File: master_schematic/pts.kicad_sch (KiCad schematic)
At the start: 27 parts, among them J10 0430450400, J2 0430450400, J3 0430450400, J4 0430450400, J5 0430450400, J6 0430450400, J7 0430450400, J8 0430450400, J9 0430450400

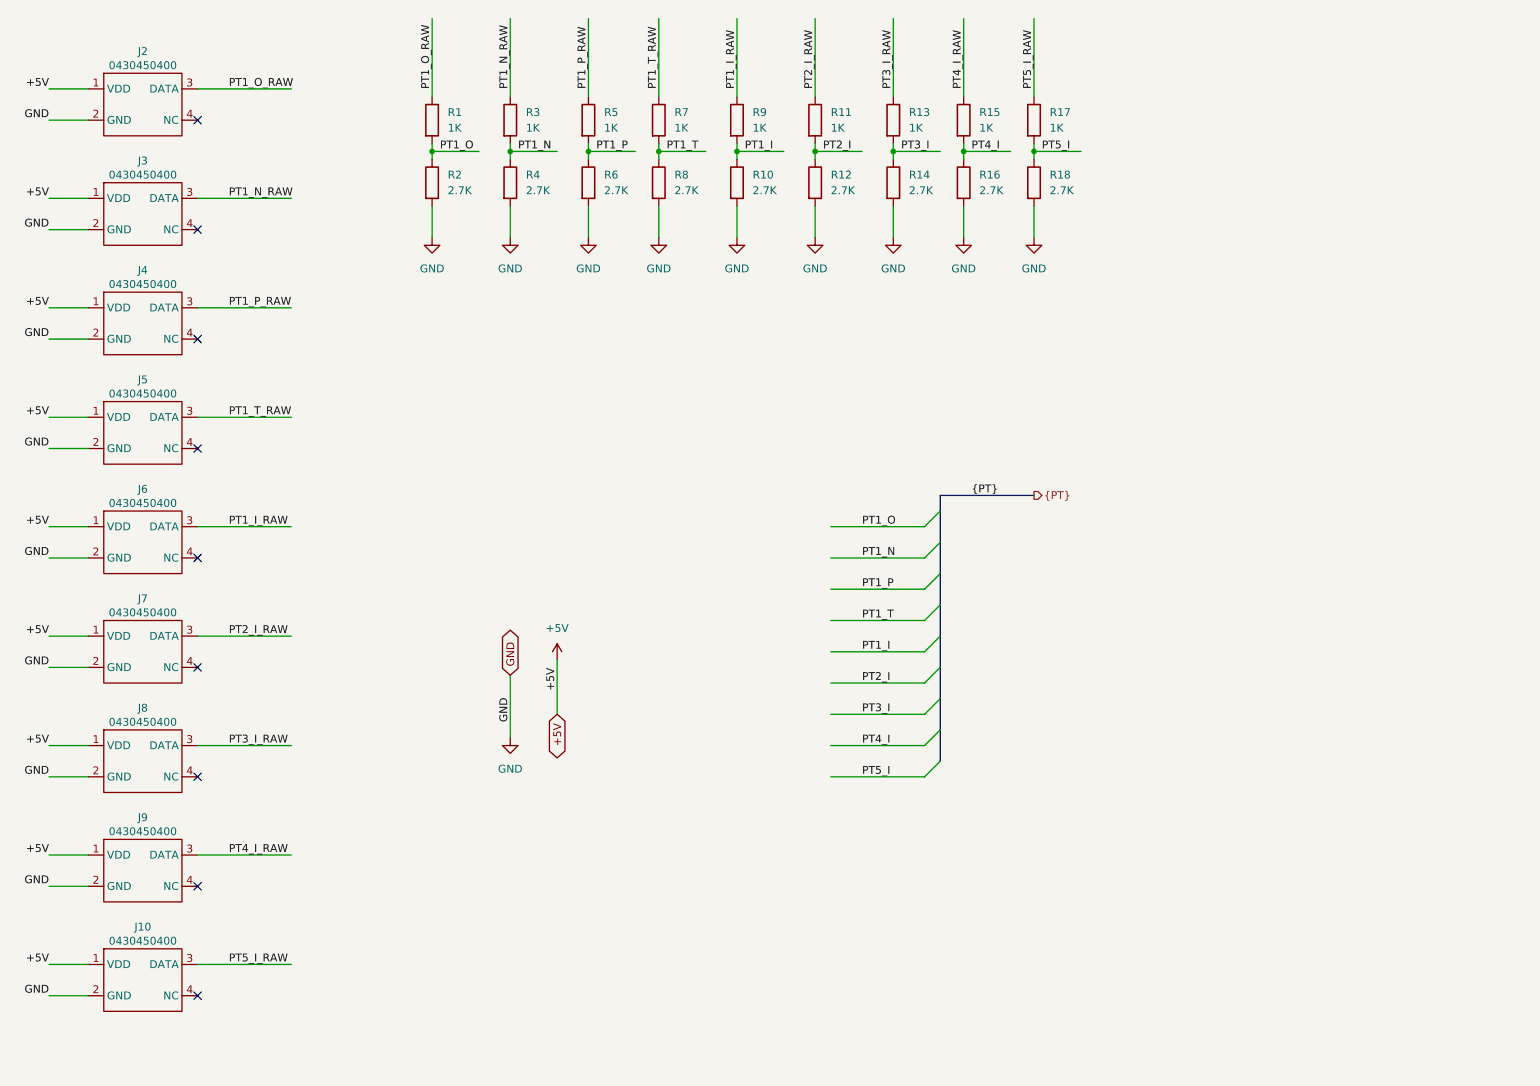
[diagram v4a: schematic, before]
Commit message: added decoupling capacitors, fixed voltage values for TTs and load cells to +3V3
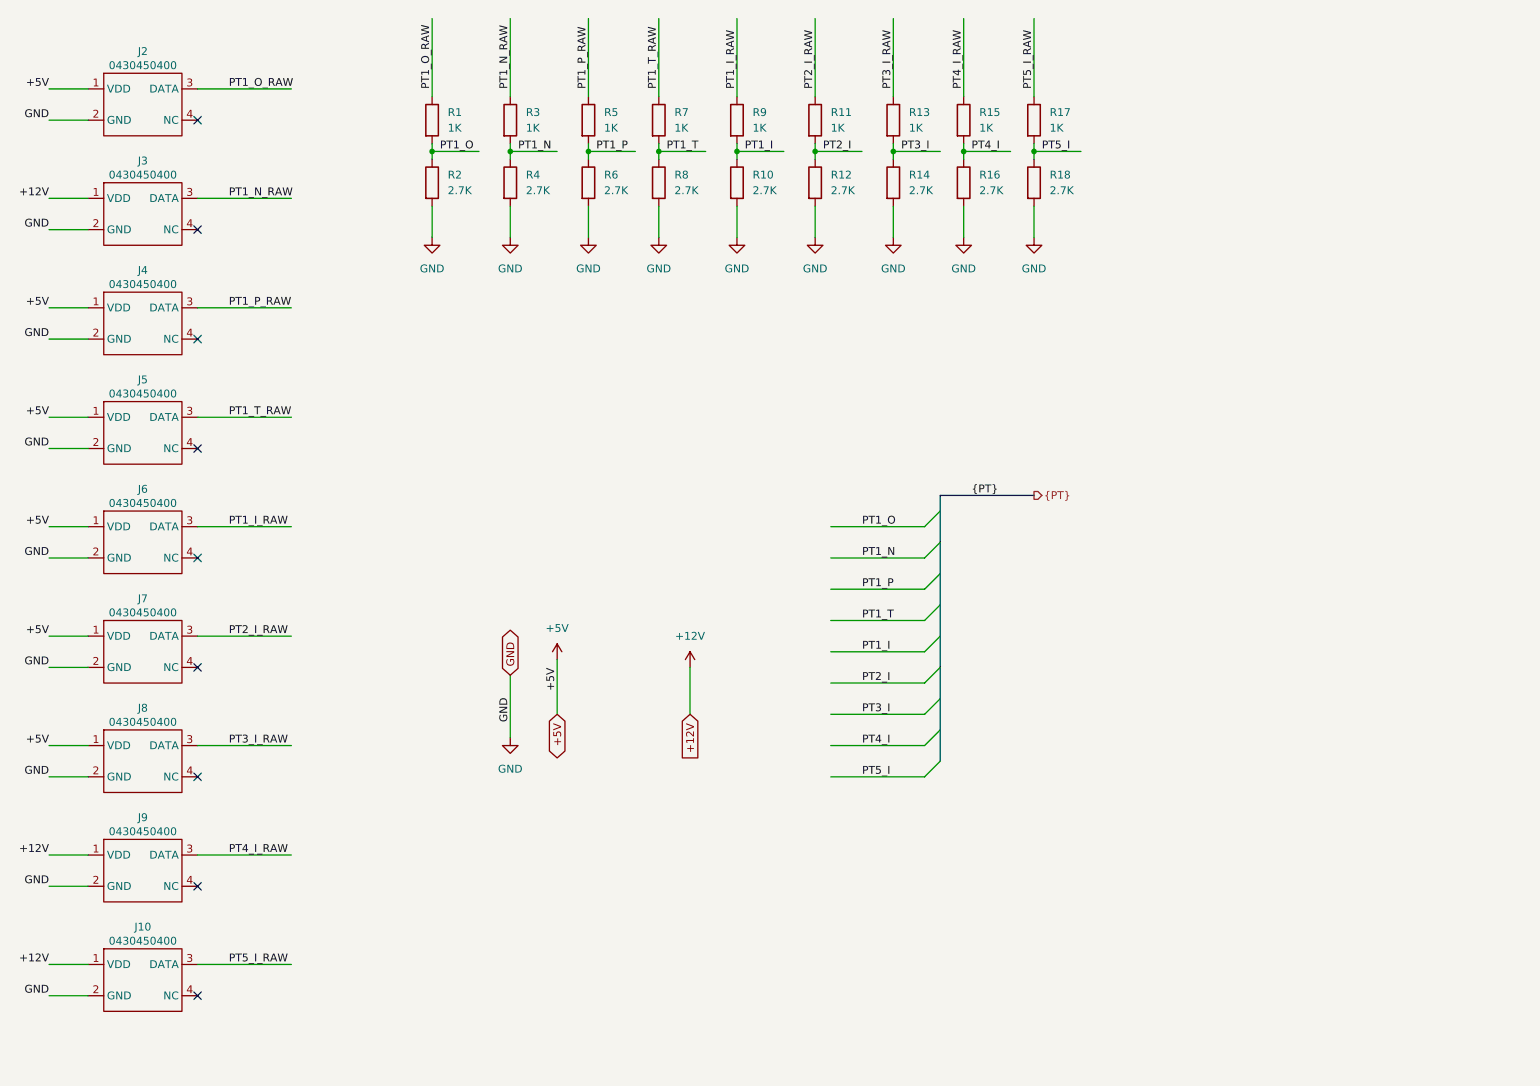
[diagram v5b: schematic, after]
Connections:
- net +5V: no longer J10.1 (VDD), J3.1 (VDD), J9.1 (VDD)
- new net +12V: J10.1 (VDD), J3.1 (VDD), J9.1 (VDD)
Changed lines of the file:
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@@
 	(wire
 		(pts
+			(xy 144.78 125.73) (xy 144.78 133.35)
+		)
+		(stroke
+			(width 0)
+			(type default)
+		)
+	)
+	(wire
+		(pts
 			(xy 177.8 20.32) (xy 177.8 33.02)
 		)
@@
 		)
 	)
-	(label "+5V"
+	(label "+12V"
 		(at 40.64 49.53 180)
 		(fields_autoplaced yes)
@@
 		)
 	)
-	(label "+5V"
+	(label "+12V"
 		(at 40.64 156.21 180)
 		(fields_autoplaced yes)
@@
 		)
 	)
-	(label "+5V"
+	(label "+12V"
 		(at 40.64 173.99 180)
 		(fields_autoplaced yes)
@@
 		)
 	)
+	(global_label "+12V"
+		(shape input)
+		(at 144.78 133.35 270)
+		(fields_autoplaced yes)
+		(effects
+			(font
+				(size 1.27 1.27)
+			)
+			(justify right)
+		)
+		(property "Intersheetrefs" "${INTERSHEET_REFS}"
+			(at 144.78 141.4152 90)
+			(effects
+				(font
+					(size 1.27 1.27)
+				)
+				(justify right)
+				(hide yes)
+			)
+		)
+	)
 	(global_label "+5V"
 		(shape bidirectional)
@@
 		(dnp no)
 		(fields_autoplaced yes)
-		(property "Reference" "#PWR024"
+		(property "Reference" "#PWR027"
 			(at 189.23 62.23 0)
 			(effects
@@
 			(project "master_schematic"
 				(path "/c4f7e98c-e88d-49cc-9841-b70710a90a72/666fb9f9-c631-4136-ad00-30a1b375897d"
-					(reference "#PWR024")
+					(reference "#PWR027")
 					(unit 1)
 				)
@@
 		(dnp no)
 		(fields_autoplaced yes)
-		(property "Reference" "#PWR022"
+		(property "Reference" "#PWR025"
 			(at 165.1 62.23 0)
 			(effects
@@
 			(project "master_schematic"
 				(path "/c4f7e98c-e88d-49cc-9841-b70710a90a72/666fb9f9-c631-4136-ad00-30a1b375897d"
-					(reference "#PWR022")
+					(reference "#PWR025")
 					(unit 1)
 				)
@@
 		(dnp no)
 		(fields_autoplaced yes)
-		(property "Reference" "#PWR021"
+		(property "Reference" "#PWR024"
 			(at 152.4 62.23 0)
 			(effects
@@
 			(project "master_schematic"
 				(path "/c4f7e98c-e88d-49cc-9841-b70710a90a72/666fb9f9-c631-4136-ad00-30a1b375897d"
-					(reference "#PWR021")
+					(reference "#PWR024")
 					(unit 1)
 				)
@@
 		(dnp no)
 		(fields_autoplaced yes)
-		(property "Reference" "#PWR020"
+		(property "Reference" "#PWR022"
 			(at 139.7 62.23 0)
 			(effects
@@
 			(project "master_schematic"
 				(path "/c4f7e98c-e88d-49cc-9841-b70710a90a72/666fb9f9-c631-4136-ad00-30a1b375897d"
-					(reference "#PWR020")
+					(reference "#PWR022")
 					(unit 1)
 				)
@@
 		(dnp no)
 		(fields_autoplaced yes)
-		(property "Reference" "#PWR018"
+		(property "Reference" "#PWR020"
 			(at 123.19 128.27 0)
 			(effects
@@
 			(project "master_schematic"
 				(path "/c4f7e98c-e88d-49cc-9841-b70710a90a72/666fb9f9-c631-4136-ad00-30a1b375897d"
-					(reference "#PWR018")
+					(reference "#PWR020")
 					(unit 1)
 				)
@@
 		(dnp no)
 		(fields_autoplaced yes)
-		(property "Reference" "#PWR016"
+		(property "Reference" "#PWR018"
 			(at 115.57 62.23 0)
 			(effects
@@
 			(project "master_schematic"
 				(path "/c4f7e98c-e88d-49cc-9841-b70710a90a72/666fb9f9-c631-4136-ad00-30a1b375897d"
-					(reference "#PWR016")
+					(reference "#PWR018")
 					(unit 1)
 				)
@@
 		(dnp no)
 		(fields_autoplaced yes)
-		(property "Reference" "#PWR025"
+		(property "Reference" "#PWR028"
 			(at 200.66 62.23 0)
 			(effects
@@
 			(project "master_schematic"
 				(path "/c4f7e98c-e88d-49cc-9841-b70710a90a72/666fb9f9-c631-4136-ad00-30a1b375897d"
-					(reference "#PWR025")
+					(reference "#PWR028")
 					(unit 1)
 				)
@@
 		(dnp no)
 		(fields_autoplaced yes)
-		(property "Reference" "#PWR023"
+		(property "Reference" "#PWR026"
 			(at 177.8 62.23 0)
 			(effects
@@
 			(project "master_schematic"
 				(path "/c4f7e98c-e88d-49cc-9841-b70710a90a72/666fb9f9-c631-4136-ad00-30a1b375897d"
-					(reference "#PWR023")
+					(reference "#PWR026")
 					(unit 1)
 				)
@@
 		(dnp no)
 		(fields_autoplaced yes)
-		(property "Reference" "#PWR015"
+		(property "Reference" "#PWR017"
 			(at 102.87 62.23 0)
 			(effects
@@
 			(project "master_schematic"
 				(path "/c4f7e98c-e88d-49cc-9841-b70710a90a72/666fb9f9-c631-4136-ad00-30a1b375897d"
-					(reference "#PWR015")
+					(reference "#PWR017")
 					(unit 1)
 				)
@@
 		(dnp no)
 		(fields_autoplaced yes)
-		(property "Reference" "#PWR019"
+		(property "Reference" "#PWR021"
 			(at 128.27 62.23 0)
 			(effects
@@
 			(project "master_schematic"
 				(path "/c4f7e98c-e88d-49cc-9841-b70710a90a72/666fb9f9-c631-4136-ad00-30a1b375897d"
-					(reference "#PWR019")
+					(reference "#PWR021")
 					(unit 1)
 				)
@@
 	)
 	(symbol
+		(lib_id "power:+12V")
+		(at 144.78 125.73 0)
+		(unit 1)
+		(exclude_from_sim no)
+		(in_bom yes)
+		(on_board yes)
+		(dnp no)
+		(fields_autoplaced yes)
+		(property "Reference" "#PWR023"
+			(at 144.78 129.54 0)
+			(effects
+				(font
+					(size 1.27 1.27)
+				)
+				(hide yes)
+			)
+		)
+		(property "Value" "+12V"
+			(at 144.78 120.65 0)
+			(effects
+				(font
+					(size 1.27 1.27)
+				)
+			)
+		)
+		(property "Footprint" ""
+			(at 144.78 125.73 0)
+			(effects
+				(font
+					(size 1.27 1.27)
+				)
+				(hide yes)
+			)
+		)
+		(property "Datasheet" ""
+			(at 144.78 125.73 0)
+			(effects
+				(font
+					(size 1.27 1.27)
+				)
+				(hide yes)
+			)
+		)
+		(property "Description" "Power symbol creates a global label with name \"+12V\""
+			(at 144.78 125.73 0)
+			(effects
+				(font
+					(size 1.27 1.27)
+				)
+				(hide yes)
+			)
+		)
+		(pin "1"
+		)
+		(instances
+			(project "master_schematic"
+				(path "/c4f7e98c-e88d-49cc-9841-b70710a90a72/666fb9f9-c631-4136-ad00-30a1b375897d"
+					(reference "#PWR023")
+					(unit 1)
+				)
+			)
+		)
+	)
+	(symbol
 		(lib_id "power:GND")
 		(at 115.57 137.16 0)
@@
 		(dnp no)
 		(fields_autoplaced yes)
-		(property "Reference" "#PWR017"
+		(property "Reference" "#PWR019"
 			(at 115.57 143.51 0)
 			(effects
@@
 			(project "master_schematic"
 				(path "/c4f7e98c-e88d-49cc-9841-b70710a90a72/666fb9f9-c631-4136-ad00-30a1b375897d"
-					(reference "#PWR017")
+					(reference "#PWR019")
 					(unit 1)
 				)

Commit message: finding parts
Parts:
- R15, R17, R3: value 1K -> 2.7K; Cost @ Qty 0.066 -> 0.042; Manufacturer Part # ERA-6AEB102V -> ERJ-6GEYJ272V; Supplier Part # P1.0KDACT-ND -> P2.7KACT-ND
- R16, R18, R4: value 2.7K -> 1K; Cost @ Qty 0.042 -> 0.066; Manufacturer Part # ERJ-6GEYJ272V -> ERA-6AEB102V; Supplier Part # P2.7KACT-ND -> P1.0KDACT-ND
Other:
- note added: "Note: PT1_N, PT4_I, PT5_I has 2.7K on top and 1K at the bottom because they are getting 12V power supply."

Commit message: edits after bom
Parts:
- added J24, J25, J26, J27, J28, J29, J30, J31, J32, J33: 0430450400, symbol Connector_Generic:Conn_02x02_Odd_Even
- added J34, J35, J36, J37, J38, J39, J40, J41, J42, J43, J44, J45, J46, J47, J48, J49, J50, J51, J52, J53: 0430250400, symbol Connector_Generic:Conn_02x02_Odd_Even
- J10, J2, J3, J4, J5, J6, J7, J8, J9: Cost @ Qty 1.42 -> 1.207
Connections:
- no-connect marks 9 -> 129
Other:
- note added: "Female connectors (same as on board connector)"
- note added: "Male connectors (to make connections to board)"

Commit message: updated schematic for PT
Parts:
- R15, R17: value 2.7K -> 1K; Cost @ Qty 0.042 -> 0.066; Manufacturer Part # ERJ-6GEYJ272V -> ERA-6AEB102V; Supplier Part # P2.7KACT-ND -> P1.0KDACT-ND
- R16, R18: value 1K -> 2.7K; Cost @ Qty 0.066 -> 0.042; Manufacturer Part # ERA-6AEB102V -> ERJ-6GEYJ272V; Supplier Part # P1.0KDACT-ND -> P2.7KACT-ND
- renumbered R4 to R3, R3 to R4
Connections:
- net GND: now also R4.2; no longer R3.2
- net PT1_N: now also R3.2, R4.1; no longer R3.1, R4.2
- net PT1_N_RAW: now also R3.1; no longer R4.1
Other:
- note removed: "Note: PT1_N, PT4_I, PT5_I has 2.7K on top and 1K at the bottom because they are getting 12V power supply."
- moved on the sheet: R3, R4
